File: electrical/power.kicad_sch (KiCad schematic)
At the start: 64 parts

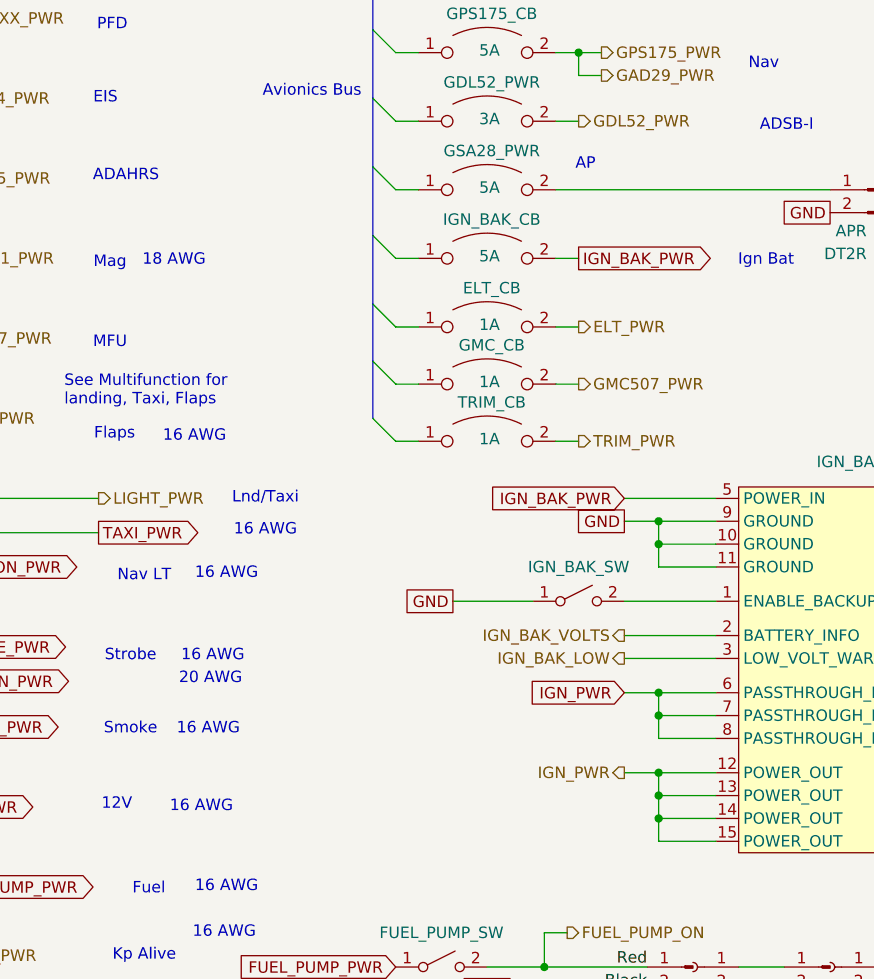
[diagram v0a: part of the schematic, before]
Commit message: Made flaps position sensor match colors of POS-12.
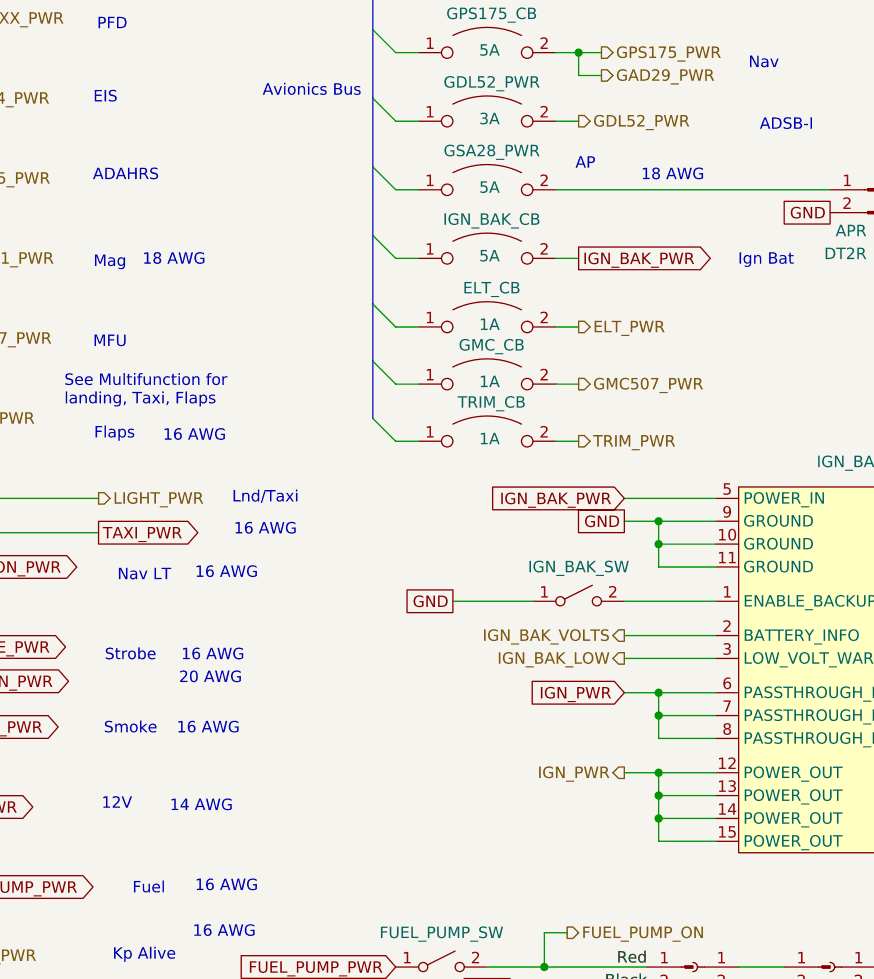
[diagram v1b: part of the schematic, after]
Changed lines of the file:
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@@
 		)
 	)
-	(text "16 AWG"
+	(text "14 AWG"
 		(exclude_from_sim no)
 		(at 109.22 132.08 0)
@@
 		(effects
 			(font
+				(size 1.27 1.27)
+			)
+		)
+	)
+	(text "18 AWG"
+		(exclude_from_sim no)
+		(at 161.593 61.976 0)
+		(effects
+			(font

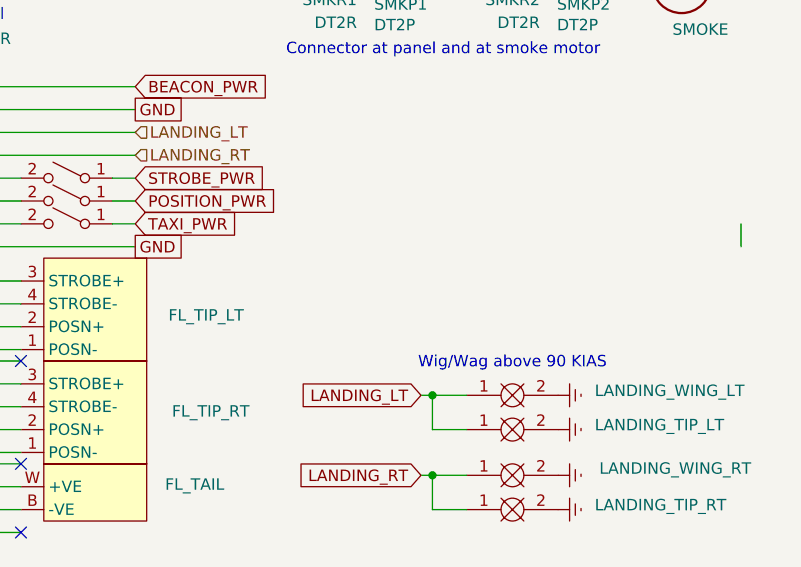
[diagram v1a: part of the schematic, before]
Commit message: Made notes about POSN+/- for Fly LED. Also, fixed Mic Lo wiring on copilot headset.
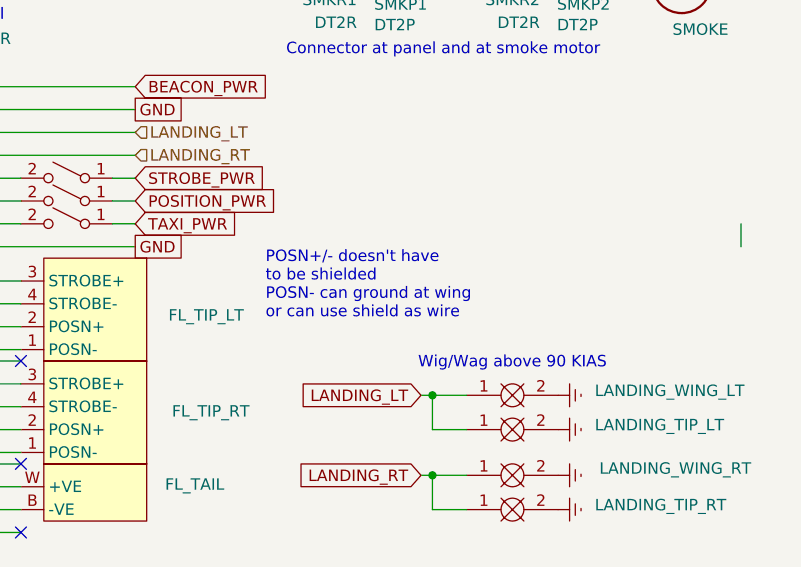
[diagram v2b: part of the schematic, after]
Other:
- note added: "POSN+/- doesn't have to be shielded POSN- can ground at wing or can use shield as wire"
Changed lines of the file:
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@@
 	(title_block
 		(title "Power Distribution")
-		(date "2026-01-03")
-		(rev "1.2.4")
+		(date "2026-01-10")
+		(rev "1.2.9")
 		(company "N877RV")
 	)
@@
 		)
 	)
+	(text "POSN+/- doesn't have\nto be shielded\nPOSN- can ground at wing\nor can use shield as wire"
+		(exclude_from_sim no)
+		(at 147.828 204.978 0)
+		(effects
+			(font
+				(size 1.27 1.27)
+			)
+			(justify left)
+		)
+	)

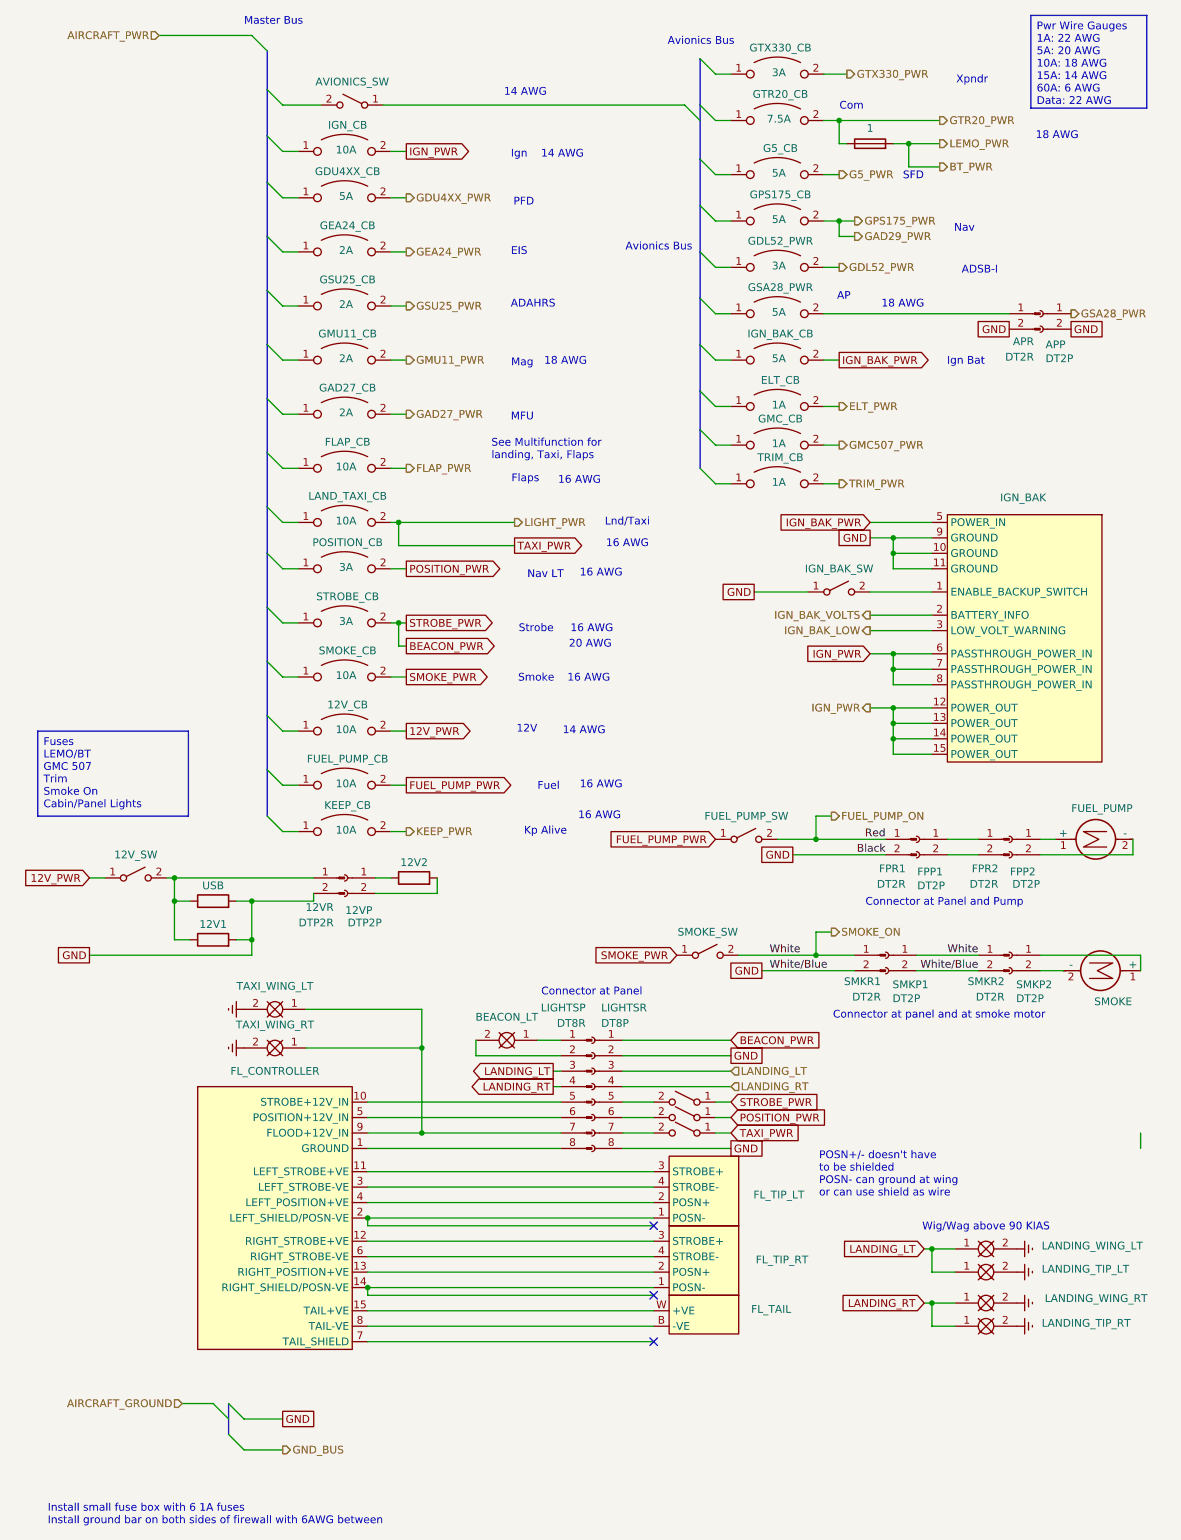
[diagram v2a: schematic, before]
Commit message: Added light power
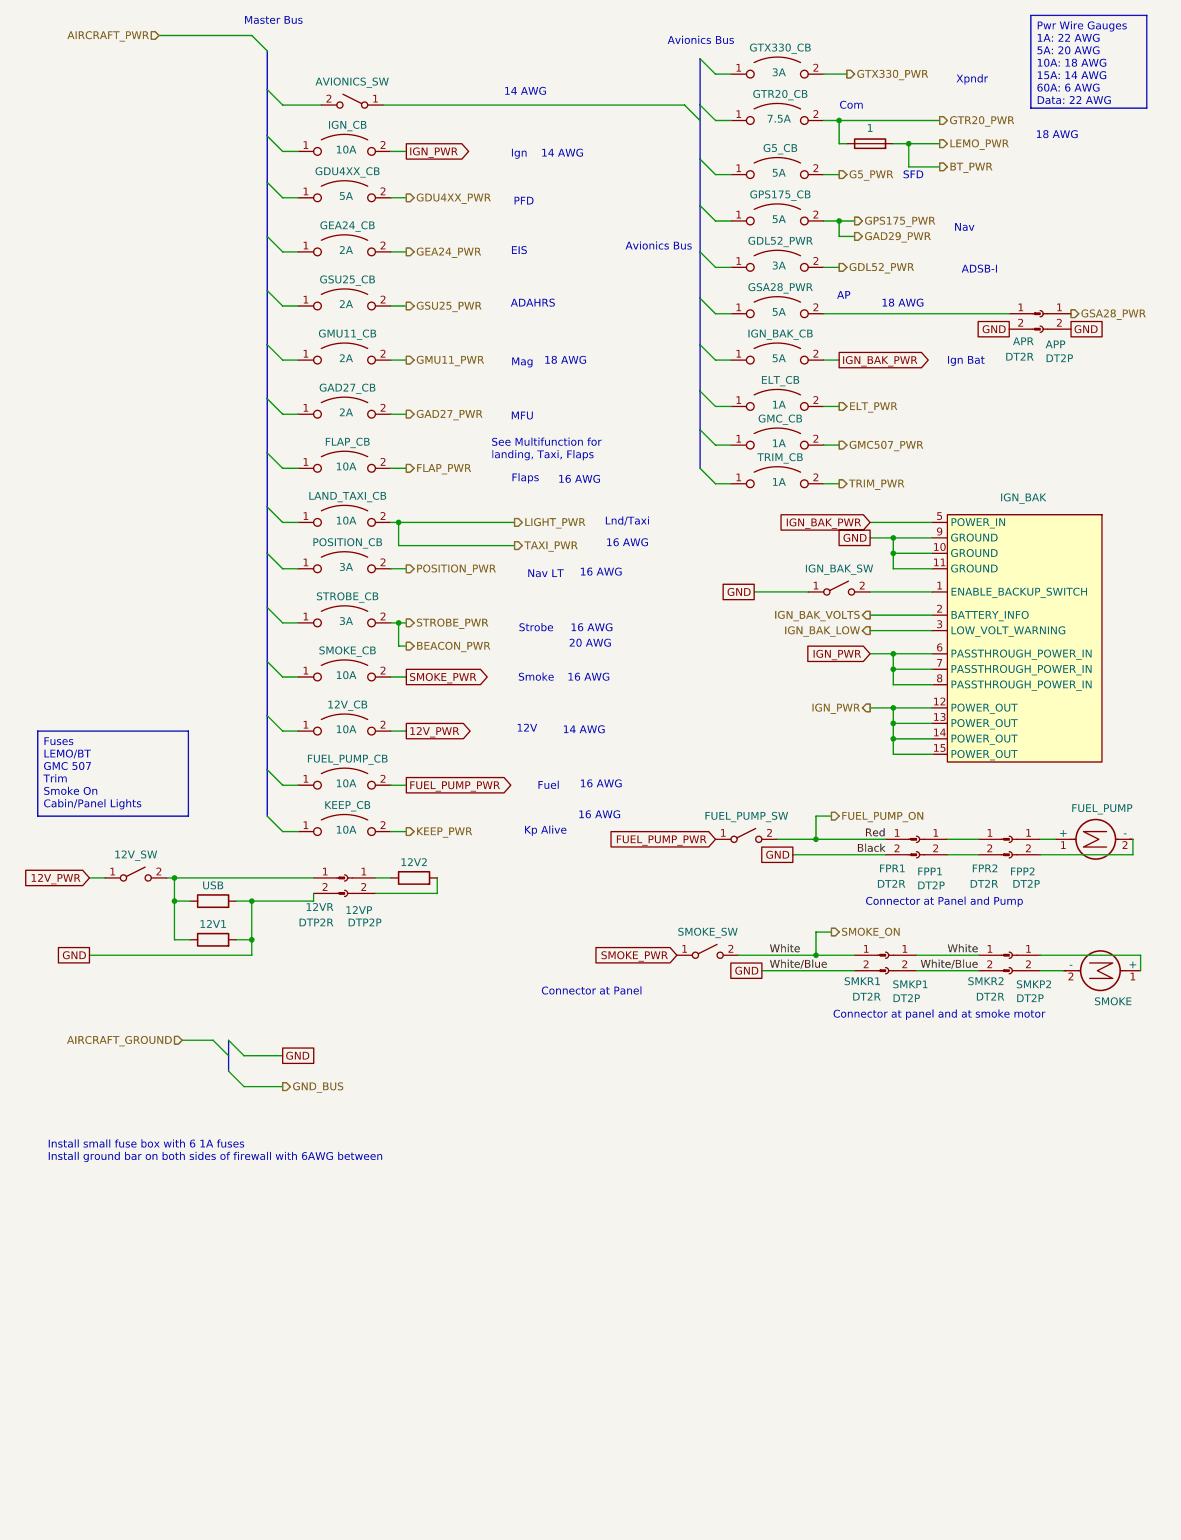
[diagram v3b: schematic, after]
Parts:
- removed BEACON_LT, TAXI_WING_LT, TAXI_WING_RT: Clear, symbol FlyerX:Bulb
- removed FL_CONTROLLER: ~, symbol flyerx:Flyleds_Strobe_Controller
- removed FL_TAIL: ~, symbol flyerx:Flyleds_Tail_Module
- removed FL_TIP_LT, FL_TIP_RT: ~, symbol flyerx:Flyleds_Wing_Module
- removed LANDING_TIP_LT, LANDING_TIP_RT, LANDING_WING_LT, LANDING_WING_RT: ~, symbol flyerx:Bulb
- removed LIGHTSP: DT8R, symbol Connector:Conn_01x08_Pin
- removed LIGHTSR: DT8P, symbol Connector:Conn_01x08_Socket
- removed POSITION_SW, STROBE_SW, TAXI_SW: ~, symbol Switch:SW_SPST
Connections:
- net TAXI_PWR renamed LIGHT_PWR
- no-connect marks 3 -> 0
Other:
- note removed: "POSN+/- doesn't have to be shielded POSN- can ground at wing or can use shield as wire"
- note removed: "Wig/Wag above 90 KIAS"
